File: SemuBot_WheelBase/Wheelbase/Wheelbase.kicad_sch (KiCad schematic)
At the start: 39 parts, among them IC1 NCP164CSN330T1G, J1 10155435-00011LF, J10 B5B-XH-A_LF__SN_, J11 B5B-XH-A_LF__SN_, J12 B5B-XH-A_LF__SN_, J13 SSW-104-01-FM-D, J3 TB003-500-P02BE, J4 B5B-XH-A_LF__SN_, J5 B5B-XH-A_LF__SN_, J6 B5B-XH-A_LF__SN_, J7 1984620, J8 1984620, J9 1984620, U1 STM32F303RET6, Y2 X322516MLB4SI

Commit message: Updating board
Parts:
- added D9: +3.3V, LED_SMD:LED_0603_1608Metric_Pad1.05x0.95mm_HandSolder, symbol Device:LED
- added J2: MTSW-103-09-L-S-400, MTSW-103-09-L-S-400:SAMTEC_MTSW-103-09-L-S-400, symbol MTSW-103-09-L-S-400:MTSW-103-09-L-S-400
- added R20: 3.3K, Resistor_SMD:R_0603_1608Metric_Pad0.98x0.95mm_HandSolder, symbol Device:R
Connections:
- net +5V: now also D9.2 (A)
- net CS_ENC_2: now also U1.15 (PA1); no longer U1.17 (PA3)
- net GND: now also J2.03, R20.2
- net USART2_TX: now reaches U1.16 (PA2)
- net USART2_TX: now also J2.01
- new net: D9.1 (K), R20.1
- new net USART2_RX: J2.02, U1.17 (PA3)
- no-connect marks 34 -> 32
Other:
- note added: "USART2"
- moved on the sheet: C1, C10, C11, C2, D3, D7, D8, H1, H2, H3, H4, IC1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

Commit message: Snapshot
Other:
- note added: "Encoders"
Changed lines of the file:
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@@
+		)
+	)
+	(text "Encoders\n"
+		(exclude_from_sim no)
+		(at 52.324 105.664 0)
+		(effects
+			(font
+				(size 1.27 1.27)
+			)
 		)
 	)

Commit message: Update
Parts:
- added D10, D11, D12: ~, LED_SMD:LED_0603_1608Metric_Pad1.05x0.95mm_HandSolder, symbol Device:LED
- added R21, R22, R23: 150, Resistor_SMD:R_0603_1608Metric_Pad0.98x0.95mm_HandSolder, symbol Device:R
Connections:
- net +3.3V: now also J13.05; no longer J13.01
- net GND: now also J13.04, J13.06, J13.07, J13.08, D10.1 (K), D11.1 (K), D12.1 (K); no longer J13.03, J13.05
- net NRST: now also J13.03; no longer J13.06
- net SWCLK: now also J13.01; no longer J13.04
- net motor2_led: now reaches U1.55 (PB3)
- net motor2_led: now also R21.1
- net motor3_led: now reaches U1.56 (PB4)
- net motor3_led: now also R22.1
- net motor1_led: now reaches U1.57 (PB5)
- net motor1_led: now also R23.1
- new net: D12.2 (A), R23.2
- new net: D11.2 (A), R22.2
- new net: D10.2 (A), R21.2
- no-connect marks 32 -> 28

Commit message: Snapshot
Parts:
- D10, D11, D12: value ~ -> red
- D7: value +24V -> red
- D8, D9: value +3.3V -> red
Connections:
- net ENABLE: now also U1.30 (PB11); no longer U1.33 (PB12)
- net MOTOR1_DIR: now also U1.29 (PB10); no longer U1.30 (PB11)
- net MOTOR3_DIR: now also U1.27 (PB1); no longer U1.28 (PB2)
- net nBRAKE: now also U1.28 (PB2); no longer U1.29 (PB10)
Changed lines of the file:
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@@
 	)
 	(no_connect
-		(at 135.89 105.41)
+		(at 135.89 133.35)
 	)
 	(no_connect
@@
 	(wire
 		(pts
-			(xy 135.89 133.35) (xy 139.7 133.35)
-		)
-		(stroke
-			(width 0)
-			(type default)
-		)
-	)
-	(wire
-		(pts
 			(xy 52.07 92.71) (xy 55.88 92.71)
 		)
@@
 	(wire
 		(pts
+			(xy 135.89 105.41) (xy 139.7 105.41)
+		)
+		(stroke
+			(width 0)
+			(type default)
+		)
+	)
+	(wire
+		(pts
 			(xy 226.06 96.52) (xy 231.14 96.52)
 		)
@@
 		)
 	)
-	(label "MOTOR1_DIR"
-		(at 139.7 130.81 0)
-		(effects
-			(font
-				(size 1.27 1.27)
-			)
-			(justify left bottom)
-		)
-	)
 	(label "CS_ENC_3"
 		(at 96.52 97.79 180)
@@
 		)
 	)
-	(label "ENABLE"
-		(at 139.7 133.35 0)
+	(label "MOTOR3_DIR"
+		(at 139.7 105.41 0)
 		(effects
 			(font
@@
 		)
 	)
+	(label "MOTOR1_DIR"
+		(at 139.7 128.27 0)
+		(effects
+			(font
+				(size 1.27 1.27)
+			)
+			(justify left bottom)
+		)
+	)
 	(label "motor2_led"
 		(at 173.99 146.05 180)
@@
 		)
 	)
+	(label "nBRAKE"
+		(at 139.7 107.95 0)
+		(effects
+			(font
+				(size 1.27 1.27)
+			)
+			(justify left bottom)
+		)
+	)
 	(label "MOTOR3_DIR"
 		(at 191.77 127 180)
@@
 		)
 	)
-	(label "nBRAKE"
-		(at 139.7 128.27 0)
-		(effects
-			(font
-				(size 1.27 1.27)
-			)
-			(justify left bottom)
-		)
-	)
 	(label "D+"
 		(at 176.53 29.21 0)
@@
 		)
 	)
-	(label "MOTOR3_DIR"
-		(at 139.7 107.95 0)
+	(label "MOTOR1_DIR"
+		(at 190.5 58.42 180)
 		(effects
 			(font
 				(size 1.27 1.27)
 			)
-			(justify left bottom)
+			(justify right bottom)
 		)
 	)
-	(label "MOTOR1_DIR"
-		(at 190.5 58.42 180)
+	(label "ENABLE"
+		(at 139.7 130.81 0)
 		(effects
 			(font
 				(size 1.27 1.27)
 			)
-			(justify right bottom)
+			(justify left bottom)
 		)
 	)
@@
 			)
 		)
-		(property "Value" "+3.3V"
+		(property "Value" "red"
 			(at 152.4 180.6574 90)
 			(effects
@@
 			)
 		)
-		(property "Value" "~"
+		(property "Value" "red"
 			(at 165.1 161.6075 90)
 			(effects
@@
 			)
 		)
-		(property "Value" "+3.3V"
+		(property "Value" "red"
 			(at 138.43 180.6574 90)
 			(effects
@@
 			)
 		)
-		(property "Value" "~"
+		(property "Value" "red"
 			(at 189.23 161.6075 90)
 			(effects
@@
 			)
 		)
-		(property "Value" "+24V"
+		(property "Value" "red"
 			(at 166.37 180.6574 90)
 			(effects
@@
 			)
 		)
-		(property "Value" "~"
+		(property "Value" "red"
 			(at 177.8 161.6075 90)
 			(effects

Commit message: Random push
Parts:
- added R36: 1.5k, Resistor_SMD:R_0603_1608Metric_Pad0.98x0.95mm_HandSolder, symbol Device:R
- D2: value DEBUG_LED -> red
- R21, R22, R23: value 150 -> 3.3K
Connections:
- net +3.3V: now also R36.2
- net D+: now also R36.1
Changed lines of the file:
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@@
 	)
 	(junction
+		(at 154.94 90.17)
+		(diameter 0)
+		(color 0 0 0 0)
+	)
+	(junction
 		(at 41.91 179.07)
 		(diameter 0)
@@
 	(wire
 		(pts
+			(xy 154.94 90.17) (xy 160.02 90.17)
+		)
+		(stroke
+			(width 0)
+			(type default)
+		)
+	)
+	(wire
+		(pts
 			(xy 226.06 96.52) (xy 231.14 96.52)
 		)
@@
 	(wire
 		(pts
-			(xy 140.97 90.17) (xy 135.89 90.17)
+			(xy 135.89 90.17) (xy 154.94 90.17)
 		)
 		(stroke
@@
 	(wire
 		(pts
+			(xy 154.94 88.9) (xy 154.94 90.17)
+		)
+		(stroke
+			(width 0)
+			(type default)
+		)
+	)
+	(wire
+		(pts
 			(xy 240.03 26.67) (xy 243.84 26.67)
 		)
@@
 		)
 	)
-	(label "D+"
-		(at 140.97 90.17 0)
-		(effects
-			(font
-				(size 1.27 1.27)
-			)
-			(justify left bottom)
-		)
-	)
 	(label "CS_ENC_1"
 		(at 139.7 140.97 0)
@@
 		)
 	)
+	(label "D+"
+		(at 160.02 90.17 0)
+		(effects
+			(font
+				(size 1.27 1.27)
+			)
+			(justify left bottom)
+		)
+	)
 	(label "nBRAKE"
 		(at 191.77 88.9 180)
@@
 	)
 	(symbol
+		(lib_id "Device:R")
+		(at 154.94 85.09 180)
+		(unit 1)
+		(exclude_from_sim no)
+		(in_bom yes)
+		(on_board yes)
+		(dnp no)
+		(property "Reference" "R36"
+			(at 151.384 84.836 90)
+			(effects
+				(font
+					(size 1.27 1.27)
+				)
+			)
+		)
+		(property "Value" "1.5k"
+			(at 152.908 84.328 90)
+			(effects
+				(font
+					(size 1.27 1.27)
+				)
+			)
+		)
+		(property "Footprint" "Resistor_SMD:R_0603_1608Metric_Pad0.98x0.95mm_HandSolder"
+			(at 156.718 85.09 90)
+			(effects
+				(font
+					(size 1.27 1.27)
+				)
+				(hide yes)
+			)
+		)
+		(property "Datasheet" "~"
+			(at 154.94 85.09 0)
+			(effects
+				(font
+					(size 1.27 1.27)
+				)
+				(hide yes)
+			)
+		)
+		(property "Description" "Resistor"
+			(at 154.94 85.09 0)
+			(effects
+				(font
+					(size 1.27 1.27)
+				)
+				(hide yes)
+			)
+		)
+		(pin "1"
+		)
+		(pin "2"
+		)
+		(instances
+			(project "Wheelbase"
+				(path "/2be6f82a-ce65-4218-ba0d-0d538f990ed6"
+					(reference "R36")
+					(unit 1)
+				)
+			)
+		)
+	)
+	(symbol
 		(lib_id "Device:LED")
 		(at 148.59 177.8 90)
@@
 			)
 		)
-		(property "Value" "150"
+		(property "Value" "3.3K"
 			(at 163.322 150.622 90)
 			(effects
@@
 			)
 		)
-		(property "Value" "150"
+		(property "Value" "3.3K"
 			(at 187.452 150.622 90)
 			(effects
@@
 		(fields_autoplaced yes)
 		(property "Reference" "D2"
-			(at 86.36 120.9675 0)
+			(at 96.52 119.6974 90)
 			(effects
 				(font
 					(size 1.27 1.27)
 				)
+				(justify right)
 			)
 		)
-		(property "Value" "DEBUG_LED"
-			(at 88.9 120.9675 0)
+		(property "Value" "red"
+			(at 96.52 122.2374 90)
 			(effects
 				(font
 					(size 1.27 1.27)
 				)
+				(justify right)
 			)
 		)
@@
 	)
 	(symbol
+		(lib_id "power:+3.3V")
+		(at 154.94 81.28 0)
+		(unit 1)
+		(exclude_from_sim no)
+		(in_bom yes)
+		(on_board yes)
+		(dnp no)
+		(fields_autoplaced yes)
+		(property "Reference" "#PWR092"
+			(at 154.94 85.09 0)
+			(effects
+				(font
+					(size 1.27 1.27)
+				)
+				(hide yes)
+			)
+		)
+		(property "Value" "+3.3V"
+			(at 154.94 76.2 0)
+			(effects
+				(font
+					(size 1.27 1.27)
+				)
+			)
+		)
+		(property "Footprint" ""
+			(at 154.94 81.28 0)
+			(effects
+				(font
+					(size 1.27 1.27)
+				)
+				(hide yes)
+			)
+		)
+		(property "Datasheet" ""
+			(at 154.94 81.28 0)
+			(effects
+				(font
+					(size 1.27 1.27)
+				)
+				(hide yes)
+			)
+		)
+		(property "Description" "Power symbol creates a global label with name \"+3.3V\""
+			(at 154.94 81.28 0)
+			(effects
+				(font
+					(size 1.27 1.27)
+				)
+				(hide yes)
+			)
+		)
+		(pin "1"
+		)
+		(instances
+			(project "Wheelbase"
+				(path "/2be6f82a-ce65-4218-ba0d-0d538f990ed6"
+					(reference "#PWR092")
+					(unit 1)
+				)
+			)
+		)
+	)
+	(symbol
 		(lib_id "power:GND")
 		(at 226.06 96.52 0)
@@
 			)
 		)
-		(property "Value" "150"
+		(property "Value" "3.3K"
 			(at 176.022 150.622 90)
 			(effects

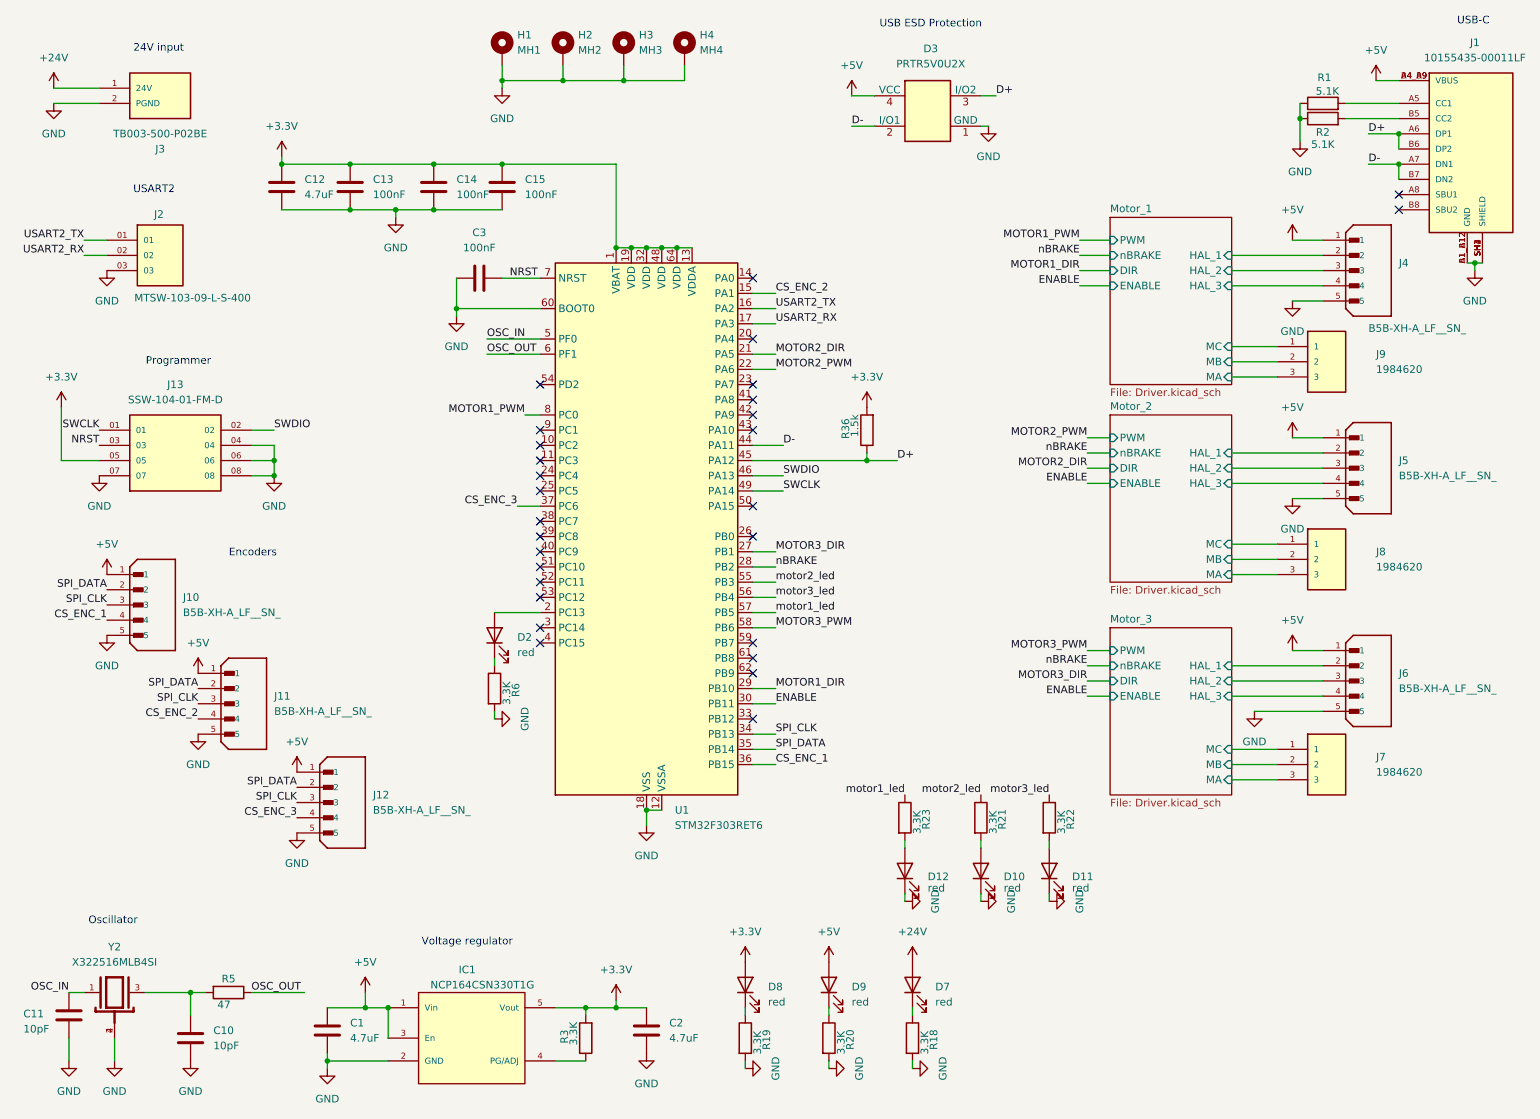
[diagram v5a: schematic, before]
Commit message: Wheelbase HW version and SPI version.
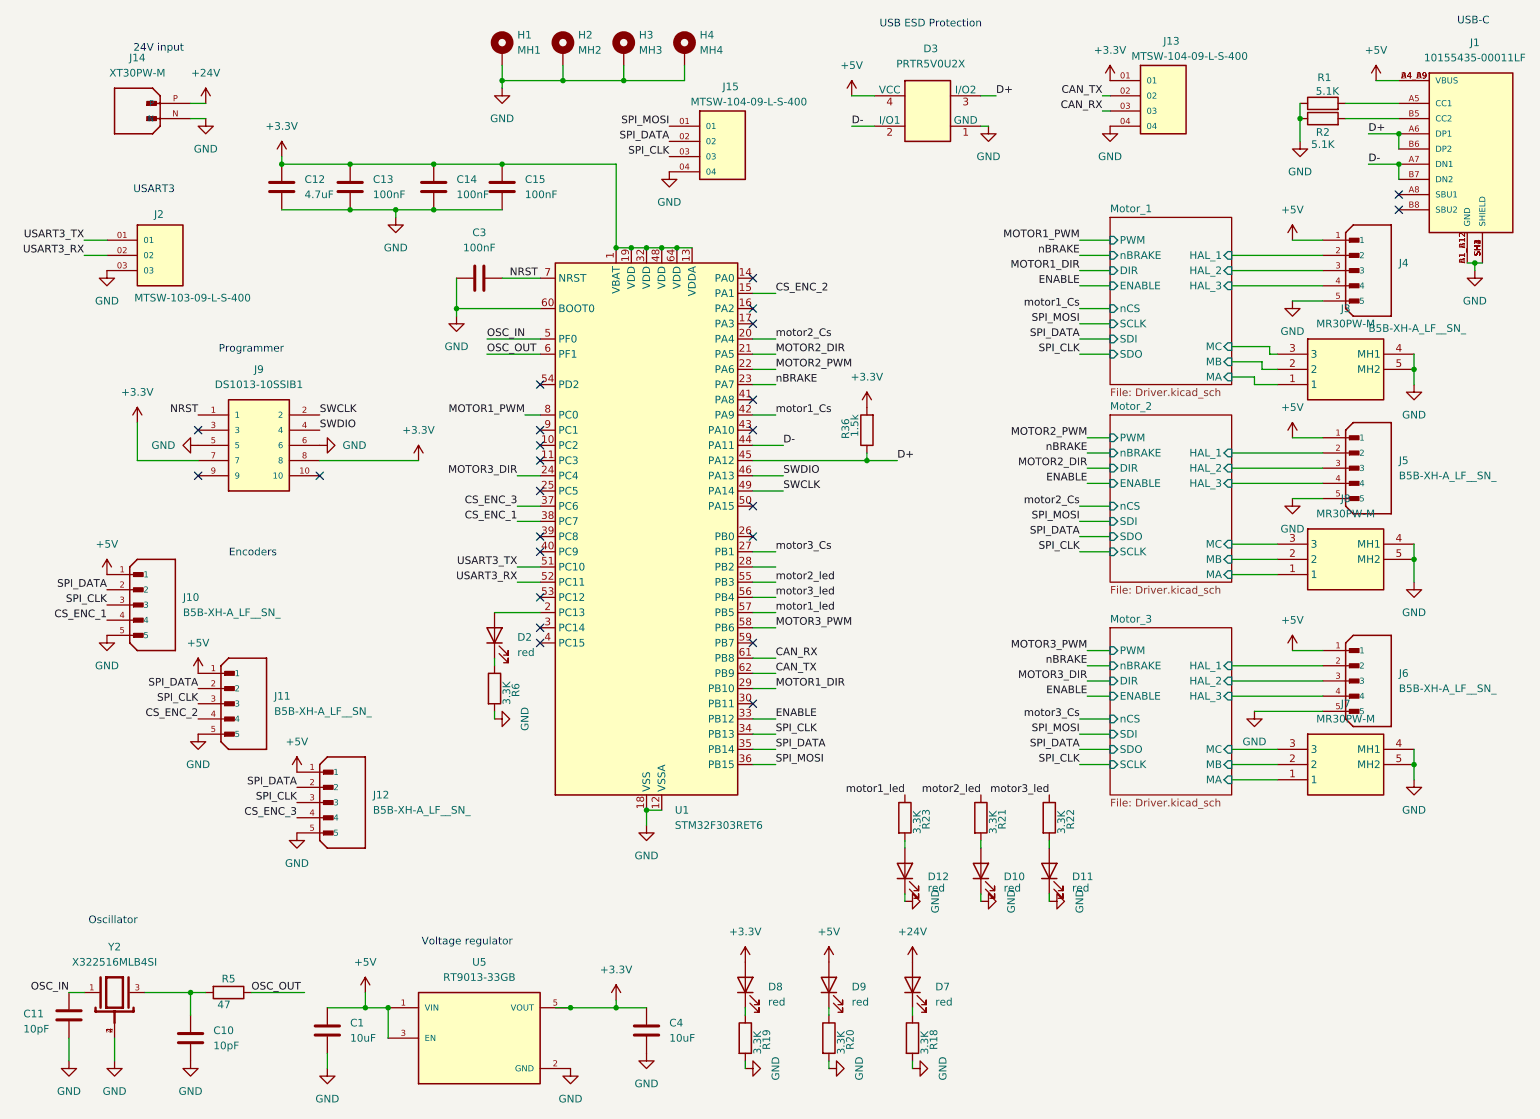
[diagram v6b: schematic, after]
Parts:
- removed C2: 4.7uF, Capacitor_SMD:C_0603_1608Metric_Pad1.08x0.95mm_HandSolder, symbol Device:C
- removed IC1: NCP164CSN330T1G, NCP164CSN330T1G:SOT95P275X110-5N, symbol NCP164CSN330T1G:NCP164CSN330T1G
- removed J13: SSW-104-01-FM-D, SSW-104-01-FM-D:SAMTEC_SSW-104-01-FM-D, symbol SSW-104-01-FM-D:SSW-104-01-FM-D
- removed J3: TB003-500-P02BE, TB003-500-P02BE:CUI_TB003-500-P02BE, symbol TB003-500-P02BE:TB003-500-P02BE
- removed J7, J8, J9: 1984620, 1984620:PHOENIX_1984620, symbol 1984620:1984620
- removed R3: 3.3K, Resistor_SMD:R_0603_1608Metric_Pad0.98x0.95mm_HandSolder, symbol Device:R
- added C4: 10uF, Capacitor_SMD:C_0805_2012Metric_Pad1.18x1.45mm_HandSolder, symbol Device:C
- added J13, J15: MTSW-104-09-L-S-400, MTSW-104-09-L-S-400:SAMTEC_MTSW-104-09-L-S-400, symbol MTSW-104-09-L-S-400:MTSW-104-09-L-S-400
- added J14: XT30PW-M, XT30:AMASS_XT30PW-M, symbol XT30PW-M:XT30PW-M
- added J3, J7, J8: MR30PW-M, MR30PWM, symbol MR30PW-M:MR30PW-M
- added J9: DS1013-10SSIB1, DS1013:CONNFLY_DS1013-10SSIB1, symbol DS1013-10SSIB1:DS1013-10SSIB1
- added U5: RT9013-33GB, RT9013:SOT94P279X129-5N, symbol RT9013-33GB:RT9013-33GB
- C1: value 4.7uF -> 10uF; footprint Capacitor_SMD:C_0603_1608Metric_Pad1.08x0.95mm_HandSolder -> Capacitor_SMD:C_0805_2012Metric_Pad1.18x1.45mm_HandSolder
- H1, H2, H3, H4: footprint MountingHole:MountingHole_2.2mm_M2_Pad_Via -> MountingHole:MountingHole_3.2mm_M3_Pad_Via
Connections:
- net +24V: now also J14.P
- net +3.3V: now also C4.2, J13.01, J9.7, J9.8, U5.5 (VOUT)
- net +5V: now also C1.2, U5.1 (VIN), U5.3 (EN); no longer C1.1
- net CS_ENC_1: now also U1.38 (PC7); no longer U1.36 (PB15)
- net ENABLE: now also U1.33 (PB12); no longer U1.30 (PB11)
- net GND: now also C1.1, C4.1, J13.04, J14.N, J15.04, J3.4 (MH1), J3.5 (MH2), J7.4 (MH1), J7.5 (MH2), J8.4 (MH1), J8.5 (MH2), J9.5, J9.6, U5.2 (GND); no longer C1.2
- net MOTOR3_DIR: now also U1.24 (PC4); no longer U1.27 (PB1)
- net Motor_1/MA: now also J3.1
- net Motor_1/MB: now also J3.2
- net Motor_1/MC: now also J3.3
- net Motor_2/MA: now also J8.1
- net Motor_2/MB: now also J8.2
- net Motor_2/MC: now also J8.3
- net Motor_3/MA: now also J7.1
- net Motor_3/MB: now also J7.2
- net Motor_3/MC: now also J7.3
- net NRST: now also J9.1
- net SPI_CLK: now also J15.03
- net SPI_DATA: now also J15.02
- net SWCLK: now also J9.2
- net SWDIO: now also J9.4
- net nBRAKE: now also U1.23 (PA7); no longer U1.28 (PB2)
- net motor2_Cs: now reaches U1.20 (PA4)
- net motor1_Cs: now reaches U1.42 (PA9)
- net USART3_TX: now reaches U1.51 (PC10)
- net USART3_TX: now also J2.01
- net USART3_RX: now reaches U1.52 (PC11)
- net USART3_RX: now also J2.02
- net CAN_RX: now reaches U1.61 (PB8)
- net CAN_RX: now also J13.03
- net CAN_TX: now reaches U1.62 (PB9)
- net CAN_TX: now also J13.02
- net USART2_RX: no longer names the net of U1.17 (PA3)
- net USART2_RX: no longer J2.02
- net USART2_TX: no longer names the net of U1.16 (PA2)
- net USART2_TX: no longer J2.01
- new net SPI_MOSI: J15.01, U1.36 (PB15)
- new net motor3_Cs: U1.27 (PB1)
- no-connect marks 28 -> 24
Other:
- sheet Motor_1 ports: added SCLK, SDI, SDO, nCS; removed none
- sheet Motor_2 ports: added SCLK, SDI, SDO, nCS; removed none
- sheet Motor_3 ports: added SCLK, SDI, SDO, nCS; removed none
- note added: "USART3"
- note removed: "USART2"

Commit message: SPI version
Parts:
- removed J2: MTSW-103-09-L-S-400, MTSW-103-09-L-S-400:SAMTEC_MTSW-103-09-L-S-400, symbol MTSW-103-09-L-S-400:MTSW-103-09-L-S-400
- added J2: MTSW-102-09-L-S-400, MTSW-102-09-L-S-400.:SAMTEC_MTSW-102-09-L-S-400, symbol MTSW-102-09-L-S-400:MTSW-102-09-L-S-400
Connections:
- net +5V: now also J2.01
- net GND: now also J2.02; no longer J15.04
- net SPI_CLK: no longer J15.03
- net SPI_DATA: no longer J15.02
- net SPI_MOSI: no longer J15.01
- net MCU_CS: now reaches U1.50 (PA15)
- net MCU_CS: now also J15.04
- net SPI3_MOSI: now reaches U1.53 (PC12)
- net SPI3_MOSI: now also J15.01
- net USART3_RX renamed SPI3_MISO
- net SPI3_MISO: now also J15.02
- net USART3_TX renamed SPI3_SCK
- net SPI3_SCK: now also J15.03
- no-connect marks 24 -> 22
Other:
- note added: "CAN"
- note added: "Debug Leds"
- note added: "Power Leds"
- note added: "SPI"
- note removed: "USART3"
- moved on the sheet: C1, C10, C11, C4, D10, D11, D12, D3, D7, D8, D9, J1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
